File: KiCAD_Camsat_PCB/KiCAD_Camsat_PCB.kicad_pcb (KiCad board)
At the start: 2 copper layers, 69.9 x 136.3 mm, 63 parts, among them J1 Barrel_Jack, J3 105017-0001, K1 HYC77-TF09-200, Q2 SS8050-G_C164885, Q9 SS8050-G_C164885, U1 ISM330DHCX, U10 BME280, U5 DHT11, U6 LM2596S-5, U7 AMS1117-3.3_C347222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

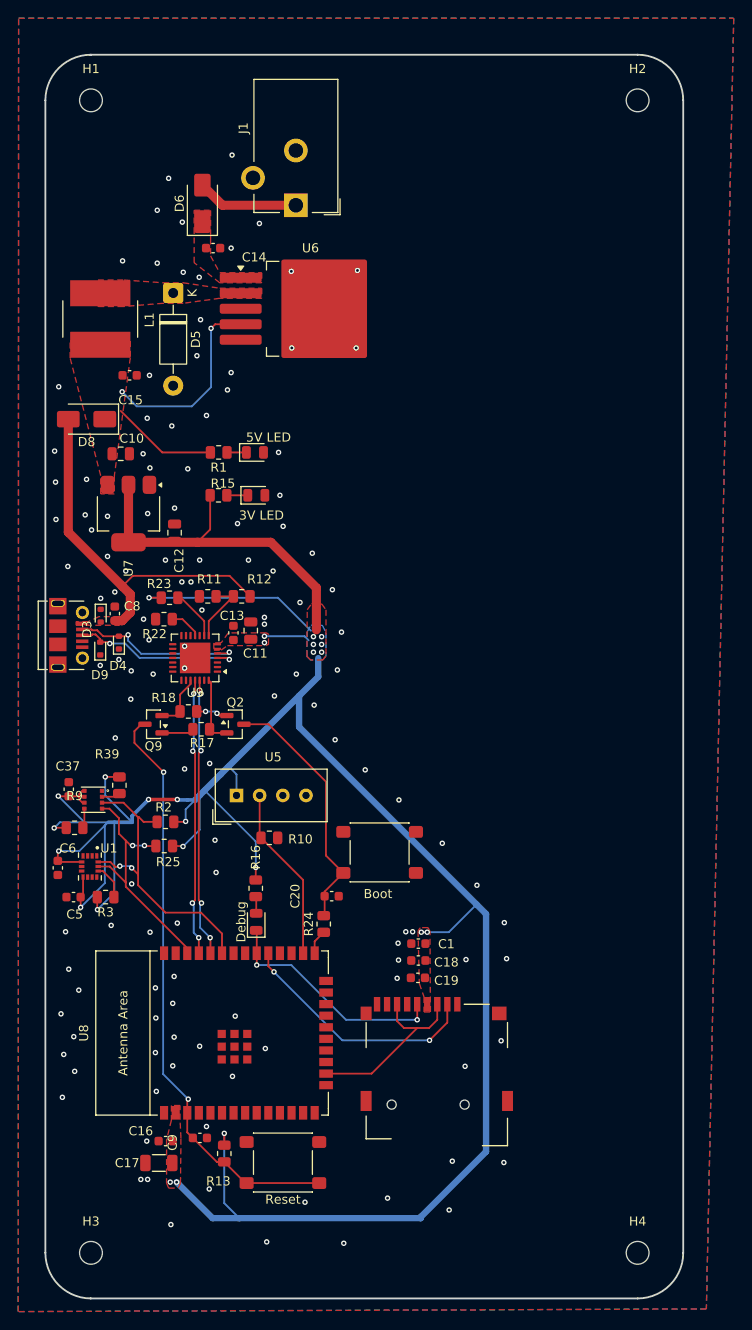
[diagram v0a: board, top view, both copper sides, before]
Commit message: Mounting Hole Size Changes
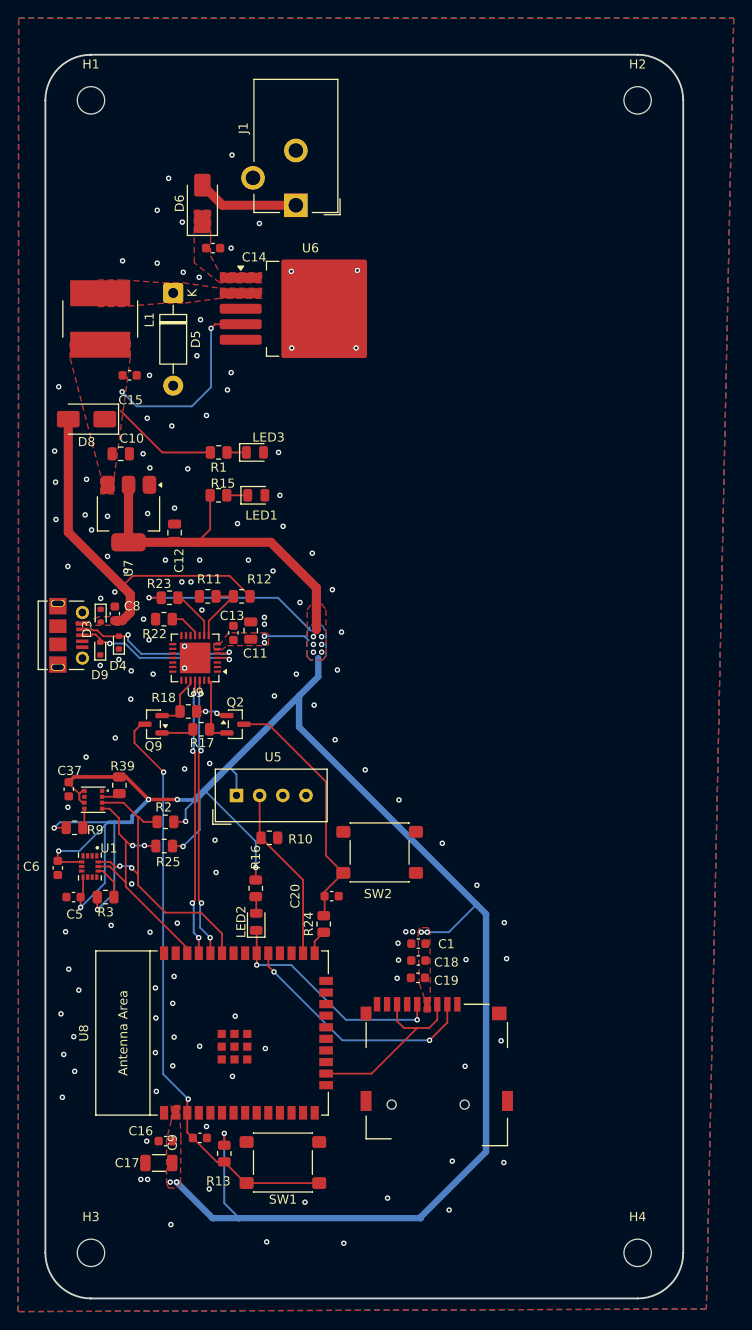
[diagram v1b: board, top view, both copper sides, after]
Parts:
- H1, H2, H3, H4: footprint MountingHole:MountingHole_2.5mm -> MountingHole:MountingHole_3mm
- LED1: renamed from 3V LED
- LED3: renamed from 5V LED
- turned C37 to -90 degrees
- renumbered Debug to LED2, Reset to SW1, Boot to SW2
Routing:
- net +3V3: track 300.1 -> 297.7 mm, vias 25 -> 23
- net GND: vias 127 -> 129

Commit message: Final Design Changes
- Updated Silkscreen
- small route updates
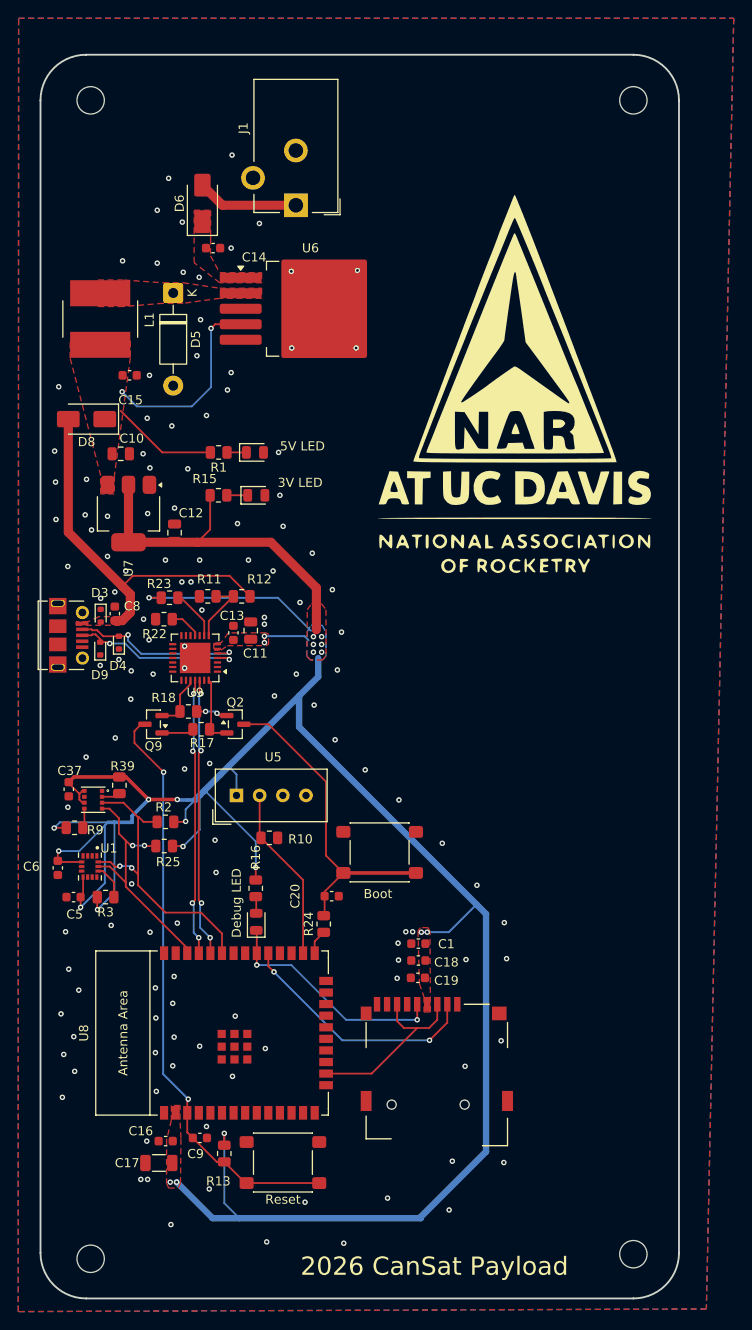
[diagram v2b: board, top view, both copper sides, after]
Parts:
- added G***: LOGO, Silkscreen_Images:NARLogo4, F.Cu at (103.0, 75.0)
- Debug LED: renamed from LED2
- moved G*** 5.00 mm to (101.6, 78.7)
- moved H3 0.65 mm to (56.5, 169.0)
- moved H4 0.49 mm to (116.0, 168.5)
- moved H2 0.46 mm to (116.0, 42.0)
- renumbered SW2 to Boot, SW1 to Reset
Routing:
- net /IO0_BTN: track 28.0 -> 35.9 mm
- net +3V3: track 297.7 -> 298.4 mm
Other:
- board size 69.9 x 136.3 mm -> 70 x 136.3 mm
- board text added: "2026 CanSat Payload"
- board text added: "3V LED"
- board text added: "5V LED"
